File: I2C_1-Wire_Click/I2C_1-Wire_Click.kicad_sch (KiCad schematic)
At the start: 16 parts, among them J1 I^{2}C to 1-Wire Click v1.0 b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, J2 1-Wire, Q1 BSS84, U1 DS2482-100

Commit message: project files updated to Kicad version 9.0.1
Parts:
- renumbered JP1 to JP2, R1 to R2, R1 to R3, R1 to R4

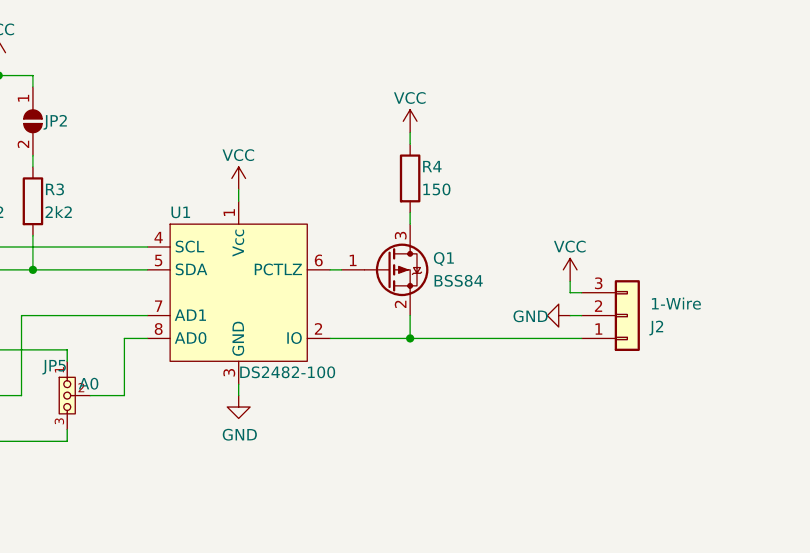
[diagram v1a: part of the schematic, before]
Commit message: HW rev 1.1 [corrected error in transistor Q1 connections]
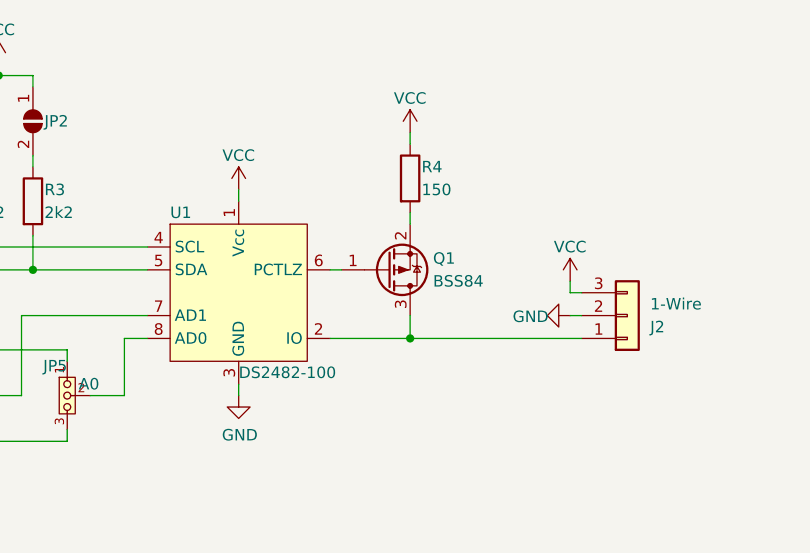
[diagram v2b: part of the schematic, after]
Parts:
- J1: value I^{2}C to 1-Wire Click v1.0 by MPro -> I^{2}C to 1-Wire Click v${REVISION} by MPro
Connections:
- net at R4.2: now also Q1.2 (S); no longer Q1.3 (D)
- net at J2.1 (Pin_1), U1.2 (IO): now also Q1.3 (D); no longer Q1.2 (S)
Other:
- company: © 2023 MPro -> © 2023-2025 MPro
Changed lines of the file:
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@@
 	(title_block
 		(title "I2C to 1-Wire Click")
-		(date "2023-08-31")
-		(rev "1.0")
-		(company "© 2023 MPro")
+		(date "2025-06-08")
+		(rev "1.1")
+		(company "© 2023-2025 MPro")
 		(comment 1 "Designed by MPro")
 		(comment 4 "Licensed under CERN-OHL-P v2 or any later version")
@@
 		(lib_id "Device:Q_PMOS_GSD")
 		(at 147.32 66.04 0)
+		(mirror x)
 		(unit 1)
 		(exclude_from_sim no)
@@
 		)
 		(property "Footprint" "footprints:SOT-23"
-			(at 152.4 63.5 0)
+			(at 152.4 68.58 0)
 			(effects
 				(font
@@
 			)
 		)
-		(property "Value" "I^{2}C to 1-Wire Click v1.0 by MPro"
+		(property "Value" "I^{2}C to 1-Wire Click v${REVISION} by MPro"
 			(at 60.96 83.185 0)
 			(effects
